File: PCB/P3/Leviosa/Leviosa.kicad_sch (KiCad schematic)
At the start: 59 parts, among them J1 Barrel_Jack, J2 2.54mm 1x03 Spare, Q1 NCE0110K, U1 TPS1H200AQDGNRQ1, U2 MC7805BD2TR4G, U3 SS495A, U4 MCP6001R, U5 LM393, U6 MX27517, U7 INA199xxDCK (50V/V)

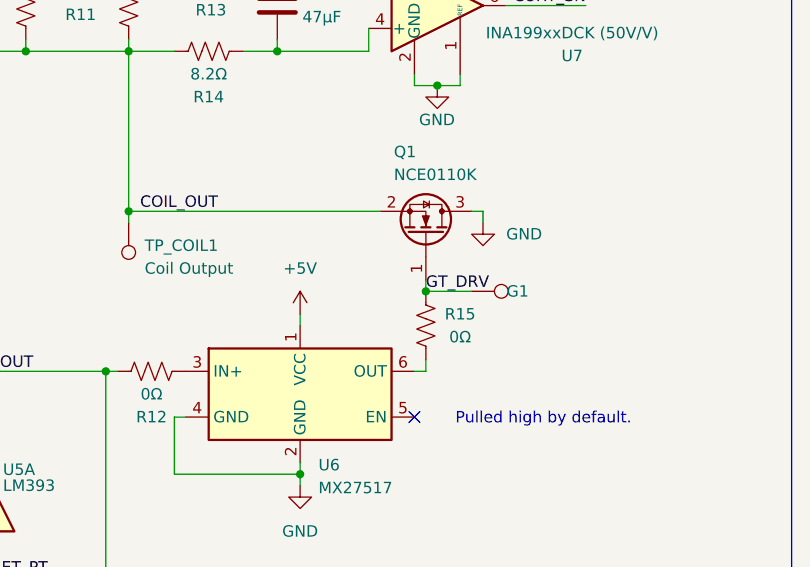
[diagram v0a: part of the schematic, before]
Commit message: add 0.1uF cap to gate driver VCC
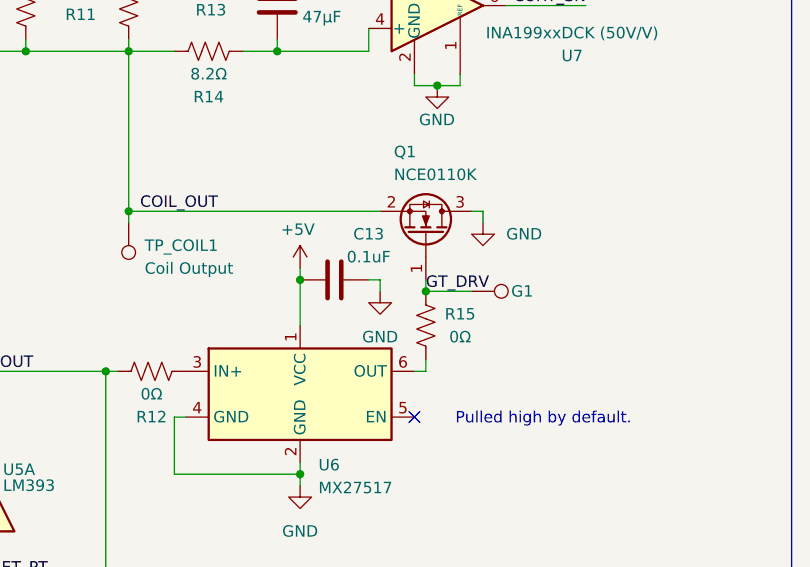
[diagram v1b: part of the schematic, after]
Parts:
- added C13: 0.1uF, Capacitor_SMD:C_0603_1608Metric, symbol Device:C
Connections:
- net +5V: now also C13.1
- net GND: now also C13.2
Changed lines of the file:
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@@
 	)
 	(junction
+		(at 226.06 90.17)
+		(diameter 0)
+		(color 0 0 0 0)
+	)
+	(junction
 		(at 223.52 54.61)
 		(diameter 0)
@@
 	(wire
 		(pts
+			(xy 234.95 90.17) (xy 233.68 90.17)
+		)
+		(stroke
+			(width 0)
+			(type default)
+		)
+	)
+	(wire
+		(pts
 			(xy 30.48 179.07) (xy 30.48 180.34)
 		)
@@
 	(wire
 		(pts
+			(xy 234.95 91.44) (xy 234.95 90.17)
+		)
+		(stroke
+			(width 0)
+			(type default)
+		)
+	)
+	(wire
+		(pts
 			(xy 173.99 53.34) (xy 173.99 54.61)
 		)
@@
 	(wire
 		(pts
-			(xy 226.06 93.98) (xy 226.06 95.25)
+			(xy 226.06 88.9) (xy 226.06 90.17)
 		)
 		(stroke
@@
 	(wire
 		(pts
+			(xy 226.06 90.17) (xy 226.06 95.25)
+		)
+		(stroke
+			(width 0)
+			(type default)
+		)
+	)
+	(wire
+		(pts
 			(xy 80.01 45.72) (xy 80.01 48.26)
 		)
@@
 	(symbol
 		(lib_id "Device:C")
+		(at 229.87 90.17 90)
+		(unit 1)
+		(exclude_from_sim no)
+		(in_bom yes)
+		(on_board yes)
+		(dnp no)
+		(property "Reference" "C13"
+			(at 233.68 85.09 90)
+			(effects
+				(font
+					(size 1.27 1.27)
+				)
+			)
+		)
+		(property "Value" "0.1uF"
+			(at 233.68 87.63 90)
+			(effects
+				(font
+					(size 1.27 1.27)
+				)
+			)
+		)
+		(property "Footprint" "Capacitor_SMD:C_0603_1608Metric"
+			(at 233.68 89.2048 0)
+			(effects
+				(font
+					(size 1.27 1.27)
+				)
+				(hide yes)
+			)
+		)
+		(property "Datasheet" "~"
+			(at 229.87 90.17 0)
+			(effects
+				(font
+					(size 1.27 1.27)
+				)
+				(hide yes)
+			)
+		)
+		(property "Description" "Unpolarized capacitor"
+			(at 229.87 90.17 0)
+			(effects
+				(font
+					(size 1.27 1.27)
+				)
+				(hide yes)
+			)
+		)
+		(pin "2"
+		)
+		(pin "1"
+		)
+		(instances
+			(project "Leviosa"
+				(path "/fe766911-203b-467c-b704-d4bd488f6c98"
+					(reference "C13")
+					(unit 1)
+				)
+			)
+		)
+	)
+	(symbol
+		(lib_id "Device:C")
 		(at 100.33 172.72 0)
 		(unit 1)
@@
 	)
 	(symbol
+		(lib_id "power:GND")
+		(at 234.95 91.44 0)
+		(unit 1)
+		(exclude_from_sim no)
+		(in_bom yes)
+		(on_board yes)
+		(dnp no)
+		(fields_autoplaced yes)
+		(property "Reference" "#PWR039"
+			(at 234.95 97.79 0)
+			(effects
+				(font
+					(size 1.27 1.27)
+				)
+				(hide yes)
+			)
+		)
+		(property "Value" "GND"
+			(at 234.95 96.52 0)
+			(effects
+				(font
+					(size 1.27 1.27)
+				)
+			)
+		)
+		(property "Footprint" ""
+			(at 234.95 91.44 0)
+			(effects
+				(font
+					(size 1.27 1.27)
+				)
+				(hide yes)
+			)
+		)
+		(property "Datasheet" ""
+			(at 234.95 91.44 0)
+			(effects
+				(font
+					(size 1.27 1.27)
+				)
+				(hide yes)
+			)
+		)
+		(property "Description" ""
+			(at 234.95 91.44 0)
+			(effects
+				(font
+					(size 1.27 1.27)
+				)
+			)
+		)
+		(pin "1"
+		)
+		(instances
+			(project "Leviosa"
+				(path "/fe766911-203b-467c-b704-d4bd488f6c98"
+					(reference "#PWR039")
+					(unit 1)
+				)
+			)
+		)
+	)
+	(symbol
 		(lib_id "Device:L")
 		(at 207.01 49.53 0)
@@
 		(dnp no)
 		(property "Reference" "G1"
-			(at 251.46 91.44 90)
+			(at 251.968 91.44 90)
 			(effects
 				(font
@@
 	(symbol
 		(lib_id "power:+5V")
-		(at 226.06 93.98 0)
+		(at 226.06 88.9 0)
 		(unit 1)
 		(exclude_from_sim no)
@@
 		(on_board yes)
 		(dnp no)
-		(fields_autoplaced yes)
 		(property "Reference" "#PWR032"
-			(at 226.06 97.79 0)
+			(at 226.06 92.71 0)
 			(effects
 				(font
@@
 		)
 		(property "Value" "+5V"
-			(at 226.06 88.9 0)
+			(at 225.806 84.582 0)
 			(effects
 				(font
@@
 		)
 		(property "Footprint" ""
-			(at 226.06 93.98 0)
+			(at 226.06 88.9 0)
 			(effects
 				(font
@@
 		)
 		(property "Datasheet" ""
-			(at 226.06 93.98 0)
+			(at 226.06 88.9 0)
 			(effects
 				(font
@@
 		)
 		(property "Description" "Power symbol creates a global label with name \"+5V\""
-			(at 226.06 93.98 0)
+			(at 226.06 88.9 0)
 			(effects
 				(font

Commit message: gerbers created
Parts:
- removed D1: BZT52C8V2 WD, Diode_SMD:D_SOD-123, symbol Device:D_Zener
- R3: value 1kΩ -> 2kΩ
- U1: footprint TPS1H200AQDGNRQ1:SOP65P490X110-9N -> Package_SO:HVSSOP-8-1EP_3x3mm_P0.65mm_EP1.57x1.89mm
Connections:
- net +12V_SF: now also D2.2 (A)
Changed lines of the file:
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@@
 	(wire
 		(pts
-			(xy 77.47 78.74) (xy 77.47 77.47)
+			(xy 77.47 67.31) (xy 77.47 78.74)
 		)
 		(stroke
@@
 	(wire
 		(pts
-			(xy 77.47 67.31) (xy 77.47 69.85)
-		)
-		(stroke
-			(width 0)
-			(type default)
-		)
-	)
-	(wire
-		(pts
 			(xy 226.06 111.76) (xy 226.06 113.03)
 		)
@@
 			)
 		)
-		(property "Value" "1kΩ"
+		(property "Value" "2kΩ"
 			(at 81.153 93.345 0)
 			(effects
@@
 			)
 		)
-		(property "Footprint" "TPS1H200AQDGNRQ1:SOP65P490X110-9N"
+		(property "Footprint" "Package_SO:HVSSOP-8-1EP_3x3mm_P0.65mm_EP1.57x1.89mm"
 			(at 43.18 64.77 0)
 			(effects
@@
 					(unit 1)
 				)
-			)
-		)
-	)
-	(symbol
-		(lib_id "Device:D_Zener")
-		(at 77.47 73.66 270)
-		(unit 1)
-		(exclude_from_sim no)
-		(in_bom yes)
-		(on_board yes)
-		(dnp no)
-		(property "Reference" "D1"
-			(at 82.804 74.422 90)
-			(effects
-				(font
-					(size 1.27 1.27)
-				)
-				(justify right)
-			)
-		)
-		(property "Value" "BZT52C8V2 WD"
-			(at 94.488 72.136 90)
-			(effects
-				(font
-					(size 1.27 1.27)
-				)
-				(justify right)
-			)
-		)
-		(property "Footprint" "Diode_SMD:D_SOD-123"
-			(at 77.47 73.66 0)
-			(effects
-				(font
-					(size 1.27 1.27)
-				)
-				(hide yes)
-			)
-		)
-		(property "Datasheet" "https://jlcpcb.com/partdetail/2479-BZT52C8V2WD/C2122"
-			(at 77.47 73.66 0)
-			(effects
-				(font
-					(size 1.27 1.27)
-				)
-				(hide yes)
-			)
-		)
-		(property "Description" ""
-			(at 77.47 73.66 0)
-			(effects
-				(font
-					(size 1.27 1.27)
-				)
-			)
-		)
-		(property "Vbr" "7.5V"
-			(at 72.898 73.406 90)
-			(effects
-				(font
-					(size 1.27 1.27)
-				)
-			)
-		)
-		(pin "1"
-		)
-		(pin "2"
-		)
-		(instances
-			(project "Leviosa"
-				(path "/fe766911-203b-467c-b704-d4bd488f6c98"
-					(reference "D1")
-					(unit 1)
-				)
